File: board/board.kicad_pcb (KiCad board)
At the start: 2 copper layers, 63.5 x 41.9 mm, 84 parts, among them J1 Molex Picoblade, J2 Conn_ARM_JTAG_SWD_10, J3 USB_B_Micro, J4 Conn_01x04_Male, J5 Screw_Terminal_01x02, Q1 AO3401A, Q2 Q_NMOS_GDS, Q3 Q_NMOS_GDS, Q4 Q_NMOS_GDS, Q5 Find one, U1 STM32F405RGTx, U2 TPS542941, U3 ELVH-100A-HANH-C-N2A5, U4 UCC2751x, U5 MX25R3235FM2xx1, U6 USBLC6-2SC6, Y1 16MHz

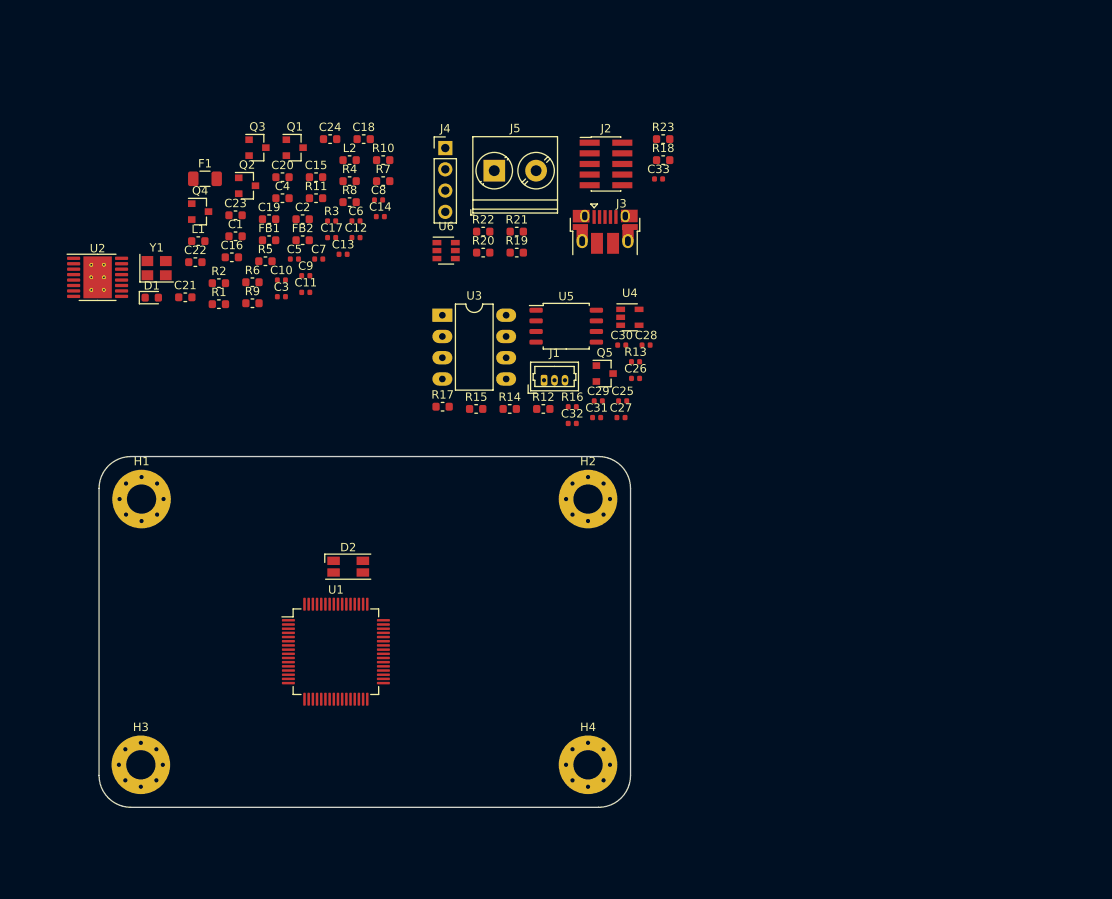
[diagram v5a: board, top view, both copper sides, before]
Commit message: Updated layout
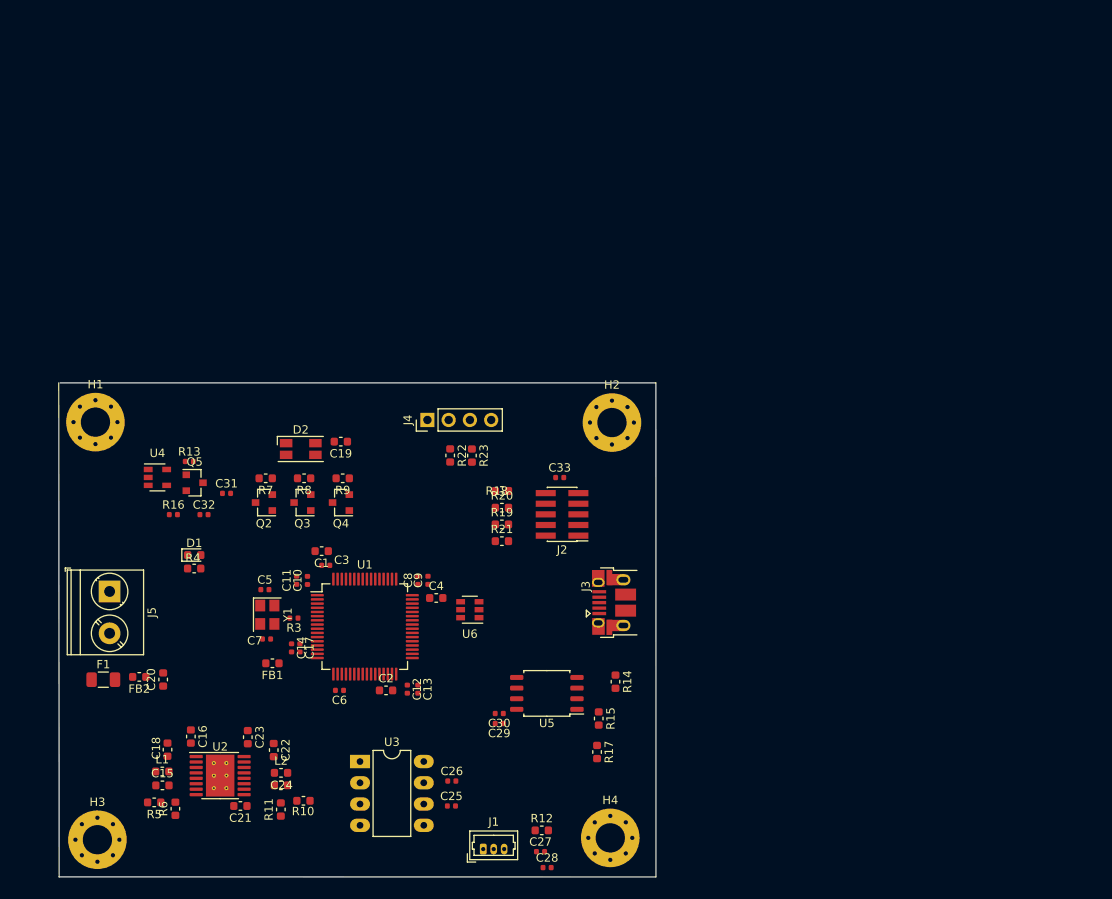
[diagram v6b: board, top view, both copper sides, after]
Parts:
- removed Q1: AO3401A, Package_TO_SOT_SMD:SOT-23
- removed R1, R2: 220, Resistor_SMD:R_0603_1608Metric
- moved C24 77.4 mm to (85.2, 128.2), turned to 180 degrees
- moved R10 77.1 mm to (87.9, 130.0)
- moved C18 76.6 mm to (71.7, 123.9), turned to 270 degrees
- moved C15 74.9 mm to (71.1, 128.2)
- moved L2 73.7 mm to (85.2, 126.7)
- moved R11 73.2 mm to (85.2, 131.1), turned to 90 degrees
- moved J5 68.1 mm to (64.8, 105.0), turned to 270 degrees
- moved R5 66.0 mm to (70.1, 130.2), turned to 180 degrees
- moved R6 63.6 mm to (72.6, 131.0), turned to 90 degrees
- moved C28 63.5 mm to (117.0, 138.0)
- moved L1 63.5 mm to (71.1, 126.5)
- moved C23 62.4 mm to (81.3, 122.4), turned to 270 degrees
- moved C20 61.7 mm to (71.2, 115.5), turned to 90 degrees
- moved U2 61.3 mm to (78.0, 127.0)
- moved C21 61.1 mm to (80.4, 130.7), turned to 180 degrees
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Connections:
- F1 pad 1: Net-(F1-Pad1) -> +UCC_VDD
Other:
- board size 63.5 x 41.9 mm -> 71.4 x 59 mm

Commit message: Update
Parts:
- removed Q4: Q_NMOS_GDS, Package_TO_SOT_SMD:SOT-23
- removed U3: ELVH-100A-HANH-C-N2A5, Package_DIP:DIP-8_W7.62mm_LongPads
- added J6: Conn_01x06_Male, Connector_PinHeader_2.54mm:PinHeader_1x06_P2.54mm_Vertical, F.Cu at (88.4, 135.7)
- added Q1: FDV305N, SOT95P240X111-3N, F.Cu at (94.4, 96.2)
- D2: value LED_RGB -> ASMB-KTF0-0A306; footprint LED_SMD:LED_RGB_1210 -> LED_SMD:LED_ASMB-KTF0-0A306
- J1: footprint Connector_Molex:Molex_PicoBlade_53047-0310_1x03_P1.25mm_Vertical -> Connector_JST:JST_XH_B3B-XH-A_1x03_P2.50mm_Vertical
- J3: footprint Connector_USB:USB_Micro-B_Amphenol_10103594-0001LF_Horizontal -> Connector_USB:USB_Micro-B_Molex_47346-0001
- Q2, Q3: value Q_NMOS_GDS -> FDV305N; footprint Package_TO_SOT_SMD:SOT-23 -> SOT95P240X111-3N
- moved D1 33.6 mm to (101.6, 121.1)
- moved R4 33.6 mm to (101.6, 122.7)
- moved R14 15.3 mm to (110.0, 118.0), turned to 0 degrees
- moved U6 7.67 mm to (115.5, 107.1)
- moved C28 7.48 mm to (117.1, 130.5), turned to 90 degrees
- moved Q2 6.80 mm to (89.8, 96.2), turned to 0 degrees
- moved C26 5.96 mm to (101.9, 132.3)
- moved C27 5.91 mm to (118.2, 130.5), turned to 270 degrees
- moved H1 4.75 mm to (67.1, 87.4)
- moved C25 4.64 mm to (101.8, 133.3)
- moved R12 4.27 mm to (112.8, 131.3)
- moved R13 4.21 mm to (76.4, 93.1)
- moved R16 4.21 mm to (74.5, 99.5)
- moved U4 4.21 mm to (72.6, 95.1)
- moved C31 4.21 mm to (80.8, 97.0)
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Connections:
- D2 pad 1: Net-(D2-Pad1) -> +3V3
- D2 pad 4: +3V3 -> Net-(D2-Pad4)
- F1 pad 1: +UCC_VDD -> Net-(F1-Pad1)
- F1 pad 2: Net-(F1-Pad2) -> +UCC_VDD
- Q2 pad 1: TIM4_CH1 -> TIM4_CH2
- Q2 pad 2: Net-(Q2-Pad2) -> PGND1
- Q2 pad 3: PGND1 -> Net-(Q2-Pad3)
- Q3 pad 1: TIM4_CH2 -> TIM4_CH3
- Q3 pad 2: Net-(Q3-Pad2) -> PGND1
- Q3 pad 3: PGND1 -> Net-(Q3-Pad3)
- R7 pad 1: Net-(Q2-Pad2) -> Net-(Q1-Pad3)
- R7 pad 2: Net-(D2-Pad1) -> Net-(D2-Pad2)
- R8 pad 1: Net-(Q3-Pad2) -> Net-(Q2-Pad3)
- R8 pad 2: Net-(D2-Pad2) -> Net-(D2-Pad4)
- R9 pad 1: Net-(Q4-Pad2) -> Net-(Q3-Pad3)
- U1 pad 51: Net-(R1-Pad2) -> USART3_TX
- U1 pad 52: Net-(R2-Pad2) -> USART3_RX
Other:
- board size 71.4 x 59 mm -> 68.6 x 58.4 mm
- copper layers 2 -> 4

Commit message: ok
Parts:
- moved R7 12.9 mm to (97.9, 91.7), turned to 0 degrees
- moved R17 11.2 mm to (114.2, 128.1)
- moved C33 7.15 mm to (111.4, 91.3)
- moved R14 7.11 mm to (114.2, 112.2), turned to 270 degrees
- moved R15 6.93 mm to (116.4, 127.3), turned to 90 degrees
- moved C30 5.98 mm to (110.8, 116.4), turned to 270 degrees
- moved C29 5.67 mm to (109.5, 116.4), turned to 270 degrees
- moved R9 5.56 mm to (88.8, 91.5), turned to 0 degrees
- moved D2 4.17 mm to (93.5, 87.2), turned to 180 degrees
- moved Q1 4.16 mm to (98.2, 94.5), turned to 180 degrees
- moved Q2 4.16 mm to (93.6, 94.5), turned to 180 degrees
- moved Q3 4.16 mm to (89.0, 94.5), turned to 180 degrees
- moved R8 3.86 mm to (93.3, 91.5), turned to 0 degrees
- moved U5 3.64 mm to (114.8, 120.1), turned to 90 degrees
- moved J4 2.97 mm to (102.6, 86.1)
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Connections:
- C1 pad 2: PGND1 -> GND
- C10 pad 2: PGND1 -> GND
- C11 pad 2: PGND1 -> GND
- C12 pad 2: PGND1 -> GND
- C13 pad 2: PGND1 -> GND
- C14 pad 2: PGND1 -> GND
- C15 pad 2: PGND1 -> GND
- C16 pad 2: PGND1 -> GND
- C17 pad 2: PGND1 -> GND
- C19 pad 1: PGND1 -> GND
- C2 pad 2: PGND1 -> GND
- C20 pad 2: PGND1 -> GND
- C21 pad 2: PGND1 -> GND
- C23 pad 2: PGND1 -> GND
- C24 pad 2: PGND1 -> GND
- C25 pad 2: PGND1 -> GND
- C26 pad 2: PGND1 -> GND
- C27 pad 2: PGND1 -> GND
- C28 pad 2: PGND1 -> GND
- C29 pad 2: PGND1 -> GND
- C3 pad 2: PGND1 -> GND
- C30 pad 2: PGND1 -> GND
- C31 pad 2: PGND1 -> GND
- C32 pad 2: PGND1 -> GND
- C33 pad 2: PGND1 -> GND
- C4 pad 2: PGND1 -> GND
- C5 pad 2: PGND1 -> GND
- C6 pad 2: PGND1 -> GND
- C7 pad 2: PGND1 -> GND
- C8 pad 2: PGND1 -> GND
- C9 pad 2: PGND1 -> GND
- J1 pad 2: PGND1 -> GND
- J2 pad 3: PGND1 -> GND
- J2 pad 5: PGND1 -> GND
- J2 pad 9: PGND1 -> GND
- J3 pad 5: PGND1 -> GND
- J4 pad 4: PGND1 -> GND
- J5 pad 2: PGND1 -> GND
- J6 pad 1: PGND1 -> GND
- Q1 pad 2: PGND1 -> GND
- Q2 pad 2: PGND1 -> GND
- Q3 pad 2: PGND1 -> GND
- Q5 pad 2: PGND1 -> GND
- R11 pad 1: PGND1 -> GND
- R17 pad 2: PGND1 -> GND
- R22 pad 1: USART3_TX -> USART3_RX
- R23 pad 1: USART3_RX -> USART3_TX
- R4 pad 1: PGND1 -> GND
- R6 pad 1: PGND1 -> GND
- U1 pad 12: PGND1 -> GND
- U1 pad 18: PGND1 -> GND
- U1 pad 46: Net-(U1-Pad46) -> SWDIO
- U1 pad 49: Net-(U1-Pad49) -> SWDCLK
- U1 pad 55: Net-(U1-Pad55) -> SWO
- U1 pad 63: PGND1 -> GND
- U2 pad 13: PGND1 -> GND
- U2 pad 4: PGND1 -> GND
- U2 pad 8: PGND1 -> GND
- U4 pad 2: PGND1 -> GND
- U5 pad 4: PGND1 -> GND
- U6 pad 2: PGND1 -> GND
- Y1 pad 2: Net-(Y1-Pad2) -> GND
- Y1 pad 4: Net-(Y1-Pad2) -> GND
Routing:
- net GND: track 0.00 -> 16.7 mm, vias 0 -> 2
- net USART3_TX: track 0.00 -> 16.6 mm
- net SPI2_!CS: track 0.00 -> 16.2 mm
- net USART3_RX: track 0.00 -> 15.6 mm
- net +3V3: track 0.00 -> 15.6 mm
- net SWDIO: track 0.00 -> 14.4 mm
- net USB_D-: track 0.00 -> 12.8 mm
- net USB_D+: track 0.00 -> 12.8 mm
- net TIM4_CH1: track 0.00 -> 10.5 mm
- net HSE_IN: track 0.00 -> 9.36 mm
- net TIM4_CH3: track 0.00 -> 9.23 mm
- net USB_CONN_D-: track 0.00 -> 8.62 mm
- net Net-(D2-Pad2): track 0.00 -> 8.52 mm
- net USB_CONN_D+: track 0.00 -> 8.13 mm
- net TIM4_CH2: track 0.00 -> 8.08 mm
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- added copper zone on B.Cu, net GND
- added copper zone on F.Cu, net GND
- added copper zone on In1.Cu, net GND
